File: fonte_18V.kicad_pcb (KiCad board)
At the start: 2 copper layers, 89.6 x 52 mm, 73 parts, among them J101 IN, J102 Conn_01x02, J401 RJ45_Shielded, J402 RJ45_Shielded, Q1 Si2308CDS, Q301 Si2308CDS, U1 LMR16030, U301 LMR16030

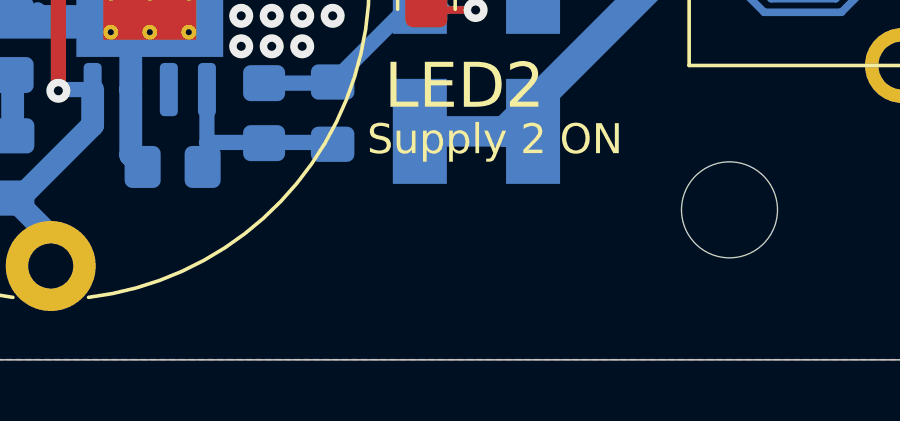
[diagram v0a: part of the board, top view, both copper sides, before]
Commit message: Silkscreen updated with JLC. Finished.
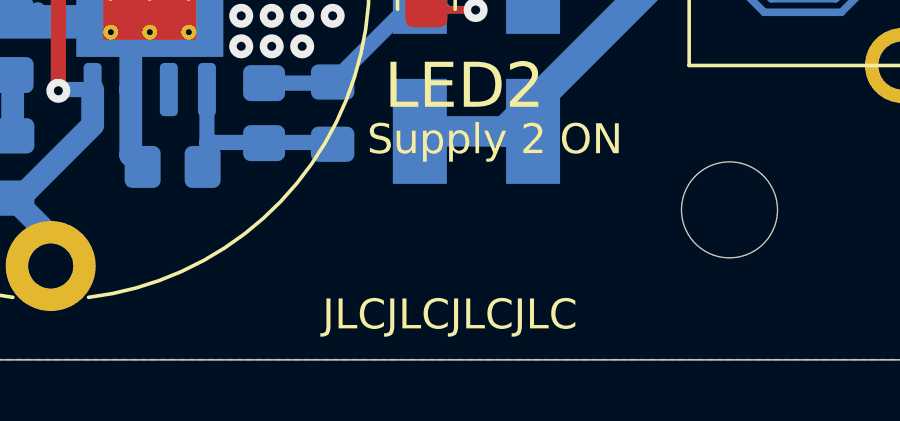
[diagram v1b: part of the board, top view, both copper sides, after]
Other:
- board text added: "JLCJLCJLCJLC"
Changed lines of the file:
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@@
+    (effects (font (size 1 1) (thickness 0.15)))
+  )
+  (gr_text "JLCJLCJLCJLC" (at 83.0834 186.69) (layer "F.SilkS")
     (effects (font (size 1 1) (thickness 0.15)))
   )
@@
     (effects (font (size 0.635 0.635) (thickness 0.15)))
   )
+  (dimension (type aligned) (layer "Dwgs.User")
+    (pts (xy 112 136.15) (xy 112 188.2))
+    (height -1.35)
+    (gr_text "52.0500 mm" (at 112.2 162.175 90) (layer "Dwgs.User")
+      (effects (font (size 1 1) (thickness 0.15)))
+    )
+    (format (units 3) (units_format 1) (precision 4))
+    (style (thickness 0.15) (arrow_length 1.27) (text_position_mode 0) (extension_height 0.58642) (extension_offset 0.5) keep_text_aligned)
+  )
+  (dimension (type aligned) (layer "Dwgs.User")
+    (pts (xy 112 188.2) (xy 22.4 188.2))
+    (height -2.95)
+    (gr_text "89.6000 mm" (at 67.2 190) (layer "Dwgs.User")
+      (effects (font (size 1 1) (thickness 0.15)))
+    )
+    (format (units 3) (units_format 1) (precision 4))
+    (style (thickness 0.15) (arrow_length 1.27) (text_position_mode 0) (extension_height 0.58642) (extension_offset 0.5) keep_text_aligned)
+  )
   (segment (start 69.553612 150.007888) (end 71.12 150.007888) (width 0.508) (layer "B.Cu") (net 1))
